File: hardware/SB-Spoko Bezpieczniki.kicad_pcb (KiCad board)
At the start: 4 copper layers, 179 x 60 mm, 143 parts, among them IC1 STM32L4P5RET6, J1 SWD, J2 Conn_02x20_Odd_Even, Q1 Q_NMOS_DGS, Q2 Q_NMOS_DGS, Q3 Q_NMOS_DGS, Q4 Q_NMOS_DGS, Q5 Q_NMOS_DGS, SW1 RESET, U1 AS222-35PN-933, U11 MCP2558FD-xSN, U12 SMART FUSE, U13 SMART FUSE, U14 SMART FUSE, U15 SMART FUSE, U16 MCP14A0052T, U17 MCP14A0052T, U18 MCP14A0052T, U2 LM2596S-12, U3 LM2596S-5, U4 LP2950-3.3_TO92, U5 VOH1016AB-T2, U6 VOH1016AB-T2, U7 VOH1016AB-T2, U8 VOH1016AB-T2, U9 VOH1016AB-T2, Y1 THE_CLOCK

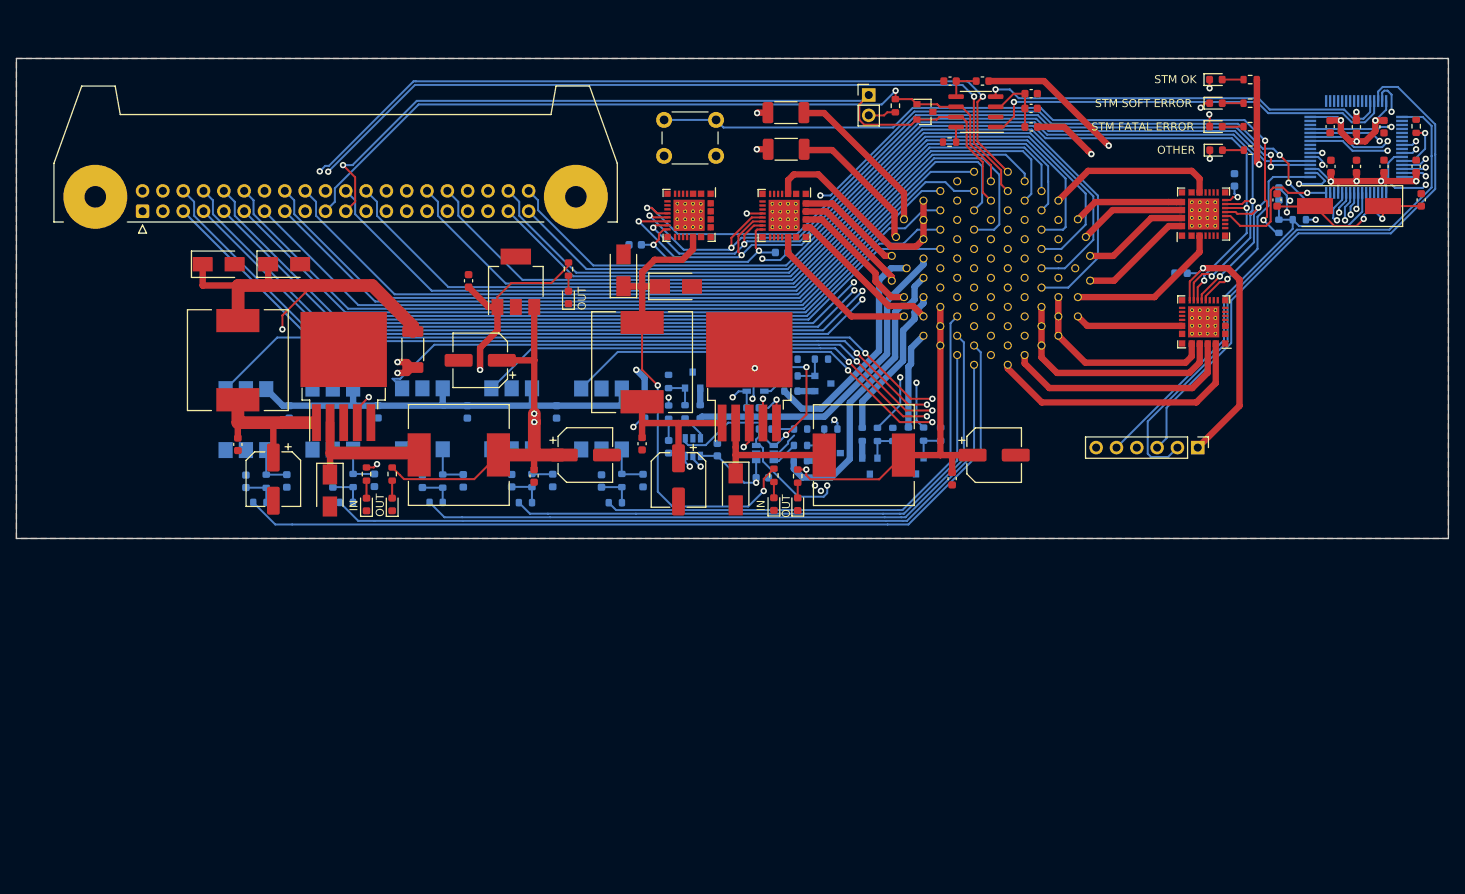
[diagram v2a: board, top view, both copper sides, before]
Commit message: changed clock and 5v converter coils, footprints rearrange commponets to fit the need now the board connector is vertical not horizontal relative to the pcb's longest side
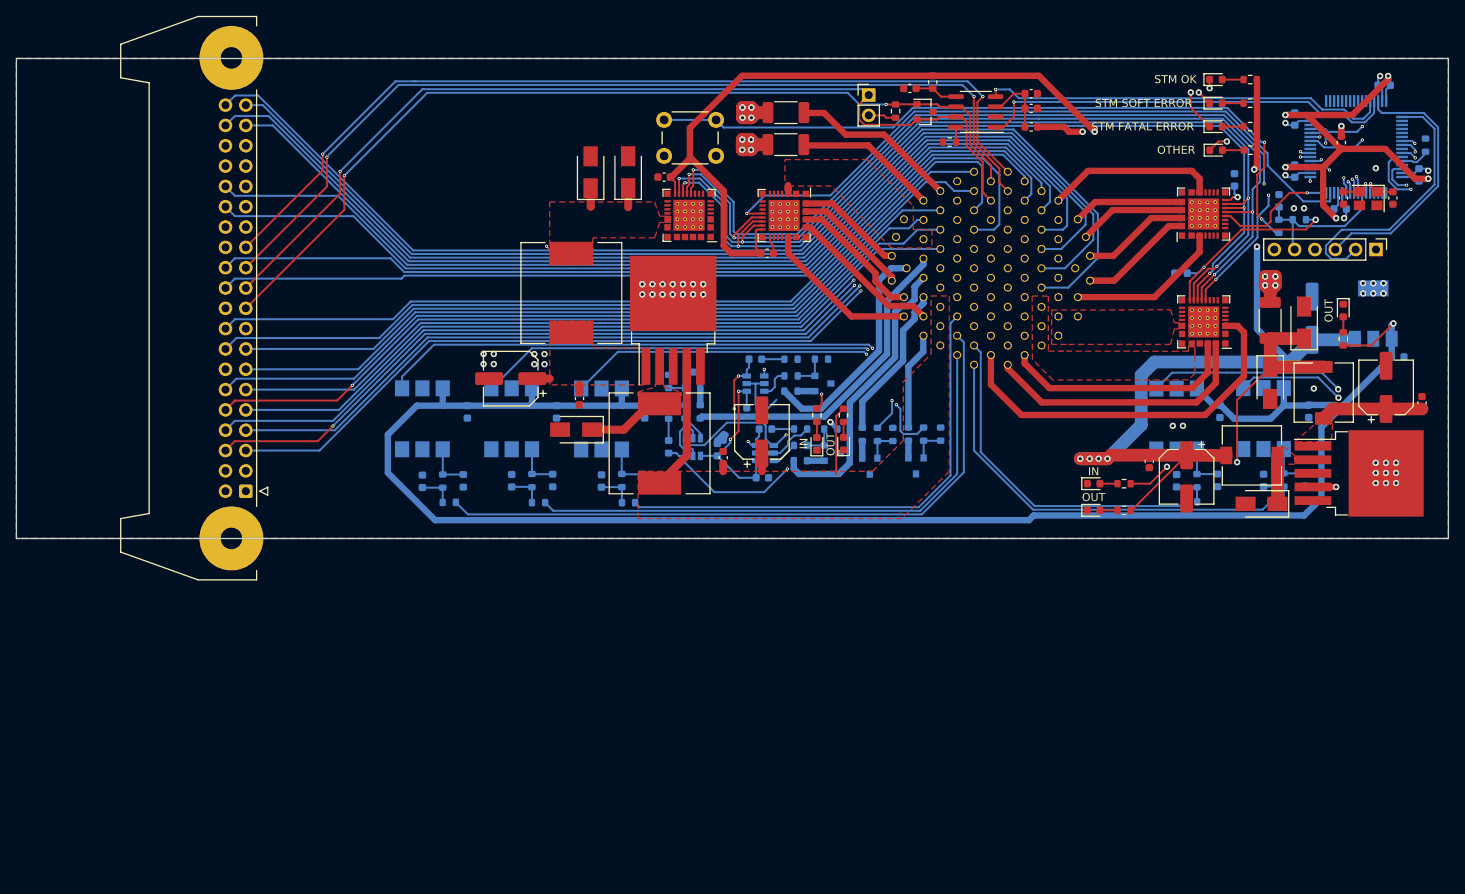
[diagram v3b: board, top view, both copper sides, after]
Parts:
- removed C41: 100nF, Capacitor_SMD:C_0603_1608Metric
- C1, C32: moved to F.Cu
- C10, C11, C12, C13, C14, C36, C37, R24, U4: moved to B.Cu
- L2, L4: footprint Inductor_SMD:L_12x12mm_H8mm -> Inductor_SMD:L_7.3x7.3_H4.5
- Y1: footprint Crystal:Crystal_SMD_HC49-SD -> Crystal:Crystal_SMD_3225-4Pin_3.2x2.5mm
- moved C3 148.1 mm to (246.7, 113.0), turned to 90 degrees
- moved C5 139.6 mm to (242.2, 111.1), turned to 90 degrees
- moved L4 135.8 mm to (234.4, 111.8)
- moved D4 132.3 mm to (227.7, 110.6), turned to -90 degrees
- moved D6 127.7 mm to (232.0, 103.0), turned to 90 degrees
- moved U3 127.5 mm to (238.8, 121.9), turned to 0 degrees
- moved C37 116.5 mm to (243.7, 107.3), turned to 0 degrees
- moved D8 116.5 mm to (226.6, 125.7), turned to 180 degrees
- moved C15 116.3 mm to (216.0, 122.8)
- moved C16 116.3 mm to (221.4, 114.1)
- moved C23 116.3 mm to (226.9, 122.7)
- moved D16 116.3 mm to (232.1, 122.7)
- moved R15 116.3 mm to (228.6, 125.4)
- moved R16 116.3 mm to (229.4, 122.7)
- moved R7 116.3 mm to (217.8, 125.4)
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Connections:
- net /CAN transreciver/+3V3_VIO renamed /Inputs/CAN transreciver/+3V3_VIO
- net /CAN transreciver/+5V_CAN_VDD renamed /Inputs/CAN transreciver/+5V_CAN_VDD
- net /CAN transreciver/SHDN renamed /Inputs/CAN transreciver/SHDN
- net /Fuse 3/VOUT_0 renamed /Fusses/Fuse 3/VOUT_0
- net /Fuse 3/VOUT_1 renamed /Fusses/Fuse 3/VOUT_1
- net /Fuse 3/VOUT_2 renamed /Fusses/Fuse 3/VOUT_2
- net /Fuse 3/VOUT_3 renamed /Fusses/Fuse 3/VOUT_3
- net /Fuse 3/VOUT_4 renamed /Fusses/Fuse 3/VOUT_4
- IC1 pad 1: 3.3V_STM_POWER -> unconnected-(IC1-Pad1)
- IC1 pad 14: Net-(IC1-Pad14) -> unconnected-(IC1-Pad14)
- IC1 pad 2: Net-(IC1-Pad2) -> unconnected-(IC1-Pad2)
- IC1 pad 24: Net-(IC1-Pad24) -> unconnected-(IC1-Pad24)
- IC1 pad 25: Net-(IC1-Pad25) -> unconnected-(IC1-Pad25)
- IC1 pad 3: Net-(IC1-Pad3) -> unconnected-(IC1-Pad3)
- IC1 pad 30: Net-(IC1-Pad30) -> unconnected-(IC1-Pad30)
- IC1 pad 33: Net-(IC1-Pad33) -> unconnected-(IC1-Pad33)
- IC1 pad 34: Net-(IC1-Pad34) -> unconnected-(IC1-Pad34)
- IC1 pad 35: Net-(IC1-Pad35) -> unconnected-(IC1-Pad35)
- IC1 pad 36: Net-(IC1-Pad36) -> unconnected-(IC1-Pad36)
- IC1 pad 37: Net-(IC1-Pad37) -> unconnected-(IC1-Pad37)
- IC1 pad 38: Net-(IC1-Pad38) -> unconnected-(IC1-Pad38)
- IC1 pad 39: Net-(IC1-Pad39) -> unconnected-(IC1-Pad39)
- IC1 pad 4: Net-(IC1-Pad4) -> unconnected-(IC1-Pad4)
- IC1 pad 40: Net-(IC1-Pad40) -> unconnected-(IC1-Pad40)
- IC1 pad 41: Net-(IC1-Pad41) -> unconnected-(IC1-Pad41)
- IC1 pad 42: Net-(IC1-Pad42) -> unconnected-(IC1-Pad42)
- IC1 pad 43: Net-(IC1-Pad43) -> unconnected-(IC1-Pad43)
- IC1 pad 50: Net-(IC1-Pad50) -> unconnected-(IC1-Pad50)
- IC1 pad 51: Net-(IC1-Pad51) -> unconnected-(IC1-Pad51)
- IC1 pad 52: Net-(IC1-Pad52) -> unconnected-(IC1-Pad52)
- IC1 pad 53: Net-(IC1-Pad53) -> unconnected-(IC1-Pad53)
- IC1 pad 54: Net-(IC1-Pad54) -> unconnected-(IC1-Pad54)
- IC1 pad 55: Net-(IC1-Pad55) -> LED_1_CONTROL
- IC1 pad 57: Net-(IC1-Pad57) -> unconnected-(IC1-Pad57)
- IC1 pad 61: LED_1_CONTROL -> unconnected-(IC1-Pad61)
- J1 pad 6: Net-(J1-Pad6) -> unconnected-(J1-Pad6)
- J2 pad 26: Net-(J2-Pad26) -> unconnected-(J2-Pad26)
- J2 pad 27: Net-(J2-Pad27) -> unconnected-(J2-Pad27)
- J2 pad 28: Net-(J2-Pad28) -> unconnected-(J2-Pad28)
- J2 pad 29: Net-(J2-Pad29) -> unconnected-(J2-Pad29)
- J2 pad 36: Net-(J2-Pad36) -> unconnected-(J2-Pad36)
- U1 pad 10: Net-(U1-Pad10) -> unconnected-(U1-Pad10)
- U1 pad 11: Net-(U1-Pad11) -> unconnected-(U1-Pad11)
- U1 pad 12: Net-(U1-Pad12) -> unconnected-(U1-Pad12)
- U1 pad 13: JETSON_??? -> unconnected-(U1-Pad13)
- U1 pad 27: Net-(U1-Pad27) -> unconnected-(U1-Pad27)
- U1 pad 31: Net-(U1-Pad31) -> unconnected-(U1-Pad31)
- U1 pad 32: Net-(U1-Pad32) -> unconnected-(U1-Pad32)
- U1 pad 33: Net-(U1-Pad33) -> unconnected-(U1-Pad33)
- U1 pad 34: WHEEL -> WS_FR
- U1 pad 35: INV_CAN+ -> INV_CAN-
- U1 pad 36: INV_CAN- -> INV_CAN+
- U1 pad 37: Net-(U1-Pad37) -> unconnected-(U1-Pad37)
- U1 pad 4: Net-(U1-Pad4) -> unconnected-(U1-Pad4)
- U1 pad 42: Net-(U1-Pad42) -> unconnected-(U1-Pad42)
- U1 pad 43: Net-(U1-Pad43) -> unconnected-(U1-Pad43)
- U1 pad 44: Net-(U1-Pad44) -> unconnected-(U1-Pad44)
- U1 pad 45: V_SAFETY -> WHEEL
- U1 pad 48: Net-(U1-Pad48) -> unconnected-(U1-Pad48)
- U1 pad 53: Net-(U1-Pad53) -> unconnected-(U1-Pad53)
- U1 pad 54: Net-(U1-Pad54) -> unconnected-(U1-Pad54)
- U1 pad 55: Net-(U1-Pad55) -> V_SAFETY
- U1 pad 64: Net-(U1-Pad64) -> unconnected-(U1-Pad64)
- U1 pad 68: RES_REF- -> WATER_P
- U1 pad 69: WATER_P -> RES_REF-
- U1 pad 7: WS_FR -> JETSON_???
- U1 pad 77: WATER_NTC_1 -> V_BSPD
- U1 pad 78: RES_SIN- -> WATER_NTC_1
- U1 pad 79: WATER_NTC_2 -> RES_SIN-
- U1 pad 81: Net-(U1-Pad81) -> unconnected-(U1-Pad81)
- U1 pad 82: Net-(U1-Pad82) -> unconnected-(U1-Pad82)
- U1 pad 86: INVERTER -> V_EBS
- U1 pad 87: INVERTER -> WATER_NTC_2
- U1 pad 9: Net-(U1-Pad9) -> unconnected-(U1-Pad9)
- U1 pad 94: V_BSPD -> INVERTER
- U1 pad 95: V_EBS -> INVERTER
- U12 pad 10: Net-(U12-Pad10) -> unconnected-(U12-Pad10)
- U12 pad 11: Net-(U12-Pad11) -> unconnected-(U12-Pad11)
- U12 pad 9: Net-(U12-Pad9) -> unconnected-(U12-Pad9)
- U13 pad 10: Net-(U13-Pad10) -> unconnected-(U13-Pad10)
- U13 pad 11: Net-(U13-Pad11) -> unconnected-(U13-Pad11)
- U13 pad 9: Net-(U13-Pad9) -> unconnected-(U13-Pad9)
- U14 pad 10: Net-(U14-Pad10) -> unconnected-(U14-Pad10)
- U14 pad 11: Net-(U14-Pad11) -> unconnected-(U14-Pad11)
- U14 pad 21: WS_FR -> JETSON_???
- U14 pad 22: WS_FR -> JETSON_???
- U14 pad 25: JETSON_??? -> INTEL_NUC
- U14 pad 26: JETSON_??? -> INTEL_NUC
- U14 pad 27: INTEL_NUC -> /Fusses/Fuse 2/VOUT_3
- U14 pad 28: INTEL_NUC -> /Fusses/Fuse 2/VOUT_3
- U14 pad 29: WHEEL -> WS_FR
- U14 pad 3: /Fuse 2/VOUT_0 -> V_SAFETY
- U14 pad 30: WHEEL -> WS_FR
- U14 pad 31: V_SAFETY -> WHEEL
- U14 pad 32: V_SAFETY -> WHEEL
- U14 pad 4: /Fuse 2/VOUT_0 -> V_SAFETY
- U14 pad 9: Net-(U14-Pad9) -> unconnected-(U14-Pad9)
- U15 pad 10: Net-(U15-Pad10) -> unconnected-(U15-Pad10)
- U15 pad 11: Net-(U15-Pad11) -> unconnected-(U15-Pad11)
- U15 pad 9: Net-(U15-Pad9) -> unconnected-(U15-Pad9)
- U5 pad 3: Net-(U5-Pad3) -> unconnected-(U5-Pad3)
- U6 pad 3: Net-(U6-Pad3) -> unconnected-(U6-Pad3)
- U7 pad 3: Net-(U7-Pad3) -> unconnected-(U7-Pad3)
- U8 pad 3: Net-(U8-Pad3) -> unconnected-(U8-Pad3)
- U9 pad 3: Net-(U9-Pad3) -> unconnected-(U9-Pad3)
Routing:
- net N_SPARE: track 171.8 -> 57.8 mm, vias 3 -> 2
- net N_TSMS: track 180.2 -> 68.4 mm, vias 3 -> 2
- net +3V3: track 345.6 -> 419.7 mm, vias 10 -> 7
- net TSMS: track 109.5 -> 42.1 mm
- net SPARE: track 94.8 -> 51.2 mm
- net WSS_FR: track 102.6 -> 142.3 mm
- net SWDIO: track 72.1 -> 33.0 mm
- net WSS_RR: track 97.3 -> 135.3 mm
- net SWCLK: track 71.0 -> 33.8 mm
- net WSS_FL: track 98.1 -> 133.9 mm
- net N_RST: track 53.7 -> 19.0 mm
- net WSS_RL: track 91.3 -> 125.8 mm
- net V_PUMP: track 58.9 -> 27.8 mm, vias 2 -> 0
- net CONVERT_5V: track 72.8 -> 42.6 mm
- net INTEL_NUC: track 29.8 -> 0.00 mm
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- added copper zone on In1.Cu, net +24V
- added copper zone on In2.Cu, net GND
- added copper zone on F.Cu, net INTEL_NUC
- added copper zone on F.Cu, net INVERTER
- added copper zone on F.Cu, net JETSON_???
- added copper zone on F.Cu, net Net-(C2-Pad1)
- added copper zone on F.Cu, net Net-(C3-Pad1)
- added copper zone on F.Cu, net Net-(D7-Pad1)
- added copper zone on F.Cu, net Net-(D8-Pad1)
- added copper zone on F.Cu, net PUMP
- added copper zone on F.Cu, net V_PUMP
- removed copper zone on In2.Cu, net +24V

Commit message: minor improvements
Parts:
- added C25: 10pF, Capacitor_SMD:CP_Elec_6.3x7.7, F.Cu at (107.2, 124.1)
- moved R19 65.6 mm to (115.8, 84.5), turned to 180 degrees
- moved JP1 57.4 mm to (120.6, 81.4)
- moved SW1 22.1 mm to (136.4, 81.2)
- moved L3 11.3 mm to (129.8, 95.2)
- moved U2 11.3 mm to (142.6, 98.6)
- moved C4 11.3 mm to (122.3, 105.9)
- moved C2 11.3 mm to (130.9, 108.4)
- moved L1 10.5 mm to (140.9, 118.1)
- moved D7 7.56 mm to (138.8, 109.1)
- moved D18 6.52 mm to (189.0, 81.5), turned to -90 degrees
- moved D6 4.24 mm to (227.7, 102.9)
- moved F4 4.24 mm to (232.0, 102.7)
- moved C32 4.11 mm to (152.0, 80.7)
- moved D3 4.11 mm to (142.8, 80.1)
- moved U15 4.11 mm to (155.1, 85.5)
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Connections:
- U1 pad 10: unconnected-(U1-Pad10) -> GND
- U1 pad 11: unconnected-(U1-Pad11) -> GND
- U1 pad 12: unconnected-(U1-Pad12) -> GND
- U1 pad 13: unconnected-(U1-Pad13) -> GND
- U1 pad 27: unconnected-(U1-Pad27) -> +24V
- U1 pad 31: unconnected-(U1-Pad31) -> AMS
- U1 pad 32: unconnected-(U1-Pad32) -> TSMS
- U1 pad 33: unconnected-(U1-Pad33) -> GND
- U1 pad 37: unconnected-(U1-Pad37) -> +24V
- U1 pad 4: unconnected-(U1-Pad4) -> GND
- U1 pad 42: unconnected-(U1-Pad42) -> HVD
- U1 pad 43: unconnected-(U1-Pad43) -> SPARE
- U1 pad 44: unconnected-(U1-Pad44) -> GND
- U1 pad 48: unconnected-(U1-Pad48) -> GND
- U1 pad 53: unconnected-(U1-Pad53) -> TD
- U1 pad 54: unconnected-(U1-Pad54) -> GND
- U1 pad 64: unconnected-(U1-Pad64) -> V_PUMP
- U1 pad 65: TSMS -> V_PUMP
- U1 pad 66: SPARE -> V_PUMP
- U1 pad 74: HVD -> BREAK_LIGHT_IN
- U1 pad 75: AMS -> GND
- U1 pad 76: TD -> V_SPARE_3
- U1 pad 81: unconnected-(U1-Pad81) -> GND
- U1 pad 82: unconnected-(U1-Pad82) -> GND
- U1 pad 83: V_PUMP -> GND
- U1 pad 84: V_PUMP -> GND
- U1 pad 85: V_PUMP -> V_SPARE_2
- U1 pad 9: unconnected-(U1-Pad9) -> GND
- U1 pad 93: BREAK_LIGHT_IN -> V_SPARE_1
- U15 pad 25: /Fusses/Fuse 3/VOUT_4 -> V_SPARE_3
- U15 pad 26: /Fusses/Fuse 3/VOUT_4 -> V_SPARE_3
- U15 pad 27: /Fusses/Fuse 3/VOUT_3 -> V_SPARE_2
- U15 pad 28: /Fusses/Fuse 3/VOUT_3 -> V_SPARE_2
- U15 pad 29: /Fusses/Fuse 3/VOUT_2 -> V_SPARE_1
- U15 pad 30: /Fusses/Fuse 3/VOUT_2 -> V_SPARE_1
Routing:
- net V_SPARE_3: track 0.00 -> 52.9 mm
- net V_SPARE_2: track 0.00 -> 45.5 mm
- net V_SPARE_1: track 0.00 -> 38.7 mm
- net Net-(R20-Pad1): track 91.3 -> 113.7 mm
- net PUMP: track 59.5 -> 73.1 mm
- net LED_2_CONTROL: track 133.1 -> 143.8 mm
- net CAR_CAN-: track 119.1 -> 129.0 mm, vias 1 -> 2
- net SS_3: track 103.3 -> 94.7 mm
- net Net-(D7-Pad1): track 9.78 -> 1.24 mm
- net AMS: track 83.7 -> 91.8 mm
- net +5V: track 303.0 -> 310.1 mm
- net BREAK_LIGHT_IN: track 12.2 -> 19.1 mm
- net TD: track 68.7 -> 75.3 mm
- net SS_0: track 86.8 -> 93.2 mm
- net Net-(D8-Pad1): track 6.05 -> 0.00 mm
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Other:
- board text added: "3.3v"
- board text added: "Designed By: Piotr Lesicki Jan Węgrzynowski Some other guy"
- board text added: "Ferrite BEAN"
- board text added: "SMART FUSES"
- board text added: "STM ???"
- board text added: "gnd"
- board text added: "n_rst"
- board text added: "swclk"
- board text added: "swdio"
- board text removed: "OTHER"
